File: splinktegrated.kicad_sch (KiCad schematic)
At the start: 60 parts, among them J1 USB_C_Receptacle_USB2.0, J10 NA_Ribbon, J11 NA_Serial, J12 NA_Conn_01x04_Female, J14 Cirque, J16 Conn_01x01_Socket, J17 Conn_01x01_Socket, J2 NA_Conn_01x04_Female, J3 NA_Conn_01x04_Female, J4 NA_Conn_01x04_Female, J5 Conn_01x02, J6 Cirque, J7 NA_trackball, J8 NA_Ribbon, J9 NA_RGB, SW1 NA_SW_SPST, SW2 NA_SW_SPST, U1 RP2040, U2 USBLC6-2P6, U3 XC6210B332MR-G, U4 USBLC6-2P6, U5 W25Q128JVS, Y1 Crystal_GND24

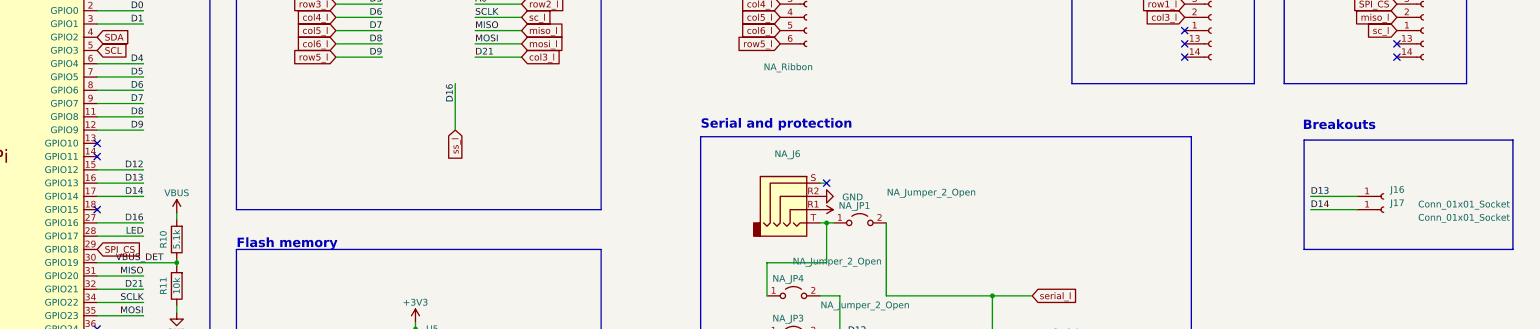
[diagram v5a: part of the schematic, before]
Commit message: add 2 breakout pins
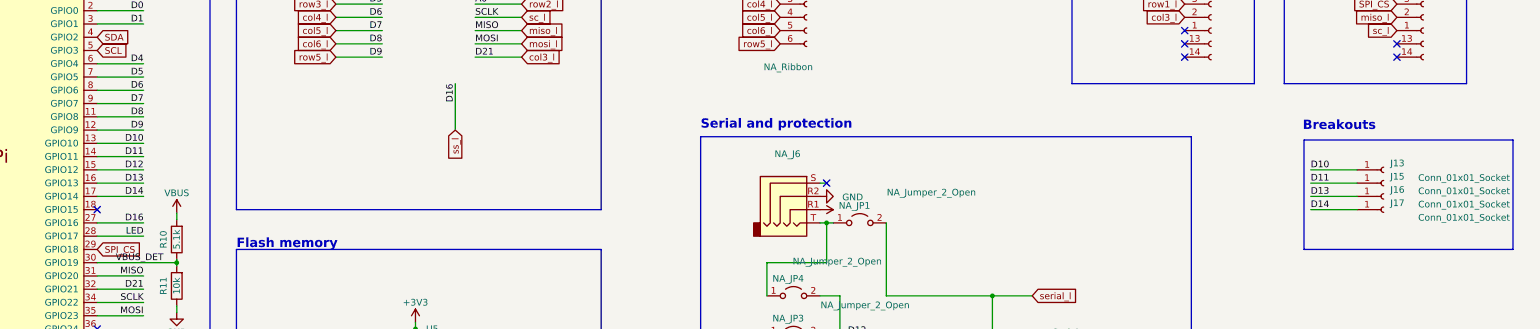
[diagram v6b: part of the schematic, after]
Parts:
- added J13, J15: Conn_01x01_Socket, local-libraries:PinHeader_1x01_P1.27mm_Vertical, symbol Connector:Conn_01x01_Socket
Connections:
- net D10: now reaches U1.13 (GPIO10)
- net D10: now also J13.1 (Pin_1)
- net D11: now reaches U1.14 (GPIO11)
- net D11: now also J15.1 (Pin_1)
- no-connect marks 18 -> 16
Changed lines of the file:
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@@
 	)
 	(no_connect
-		(at 182.88 83.82)
-	)
-	(no_connect
 		(at -88.9 60.96)
 	)
@@
 	)
 	(no_connect
-		(at 182.88 86.36)
-	)
-	(no_connect
 		(at 391.16 67.31)
 	)
@@
 	(wire
 		(pts
+			(xy 182.88 86.36) (xy 191.77 86.36)
+		)
+		(stroke
+			(width 0)
+			(type default)
+		)
+	)
+	(wire
+		(pts
 			(xy 121.92 185.42) (xy 130.81 185.42)
 		)
@@
 	(wire
 		(pts
+			(xy 424.18 91.44) (xy 415.29 91.44)
+		)
+		(stroke
+			(width 0)
+			(type default)
+		)
+	)
+	(wire
+		(pts
 			(xy -85.09 48.26) (xy -88.9 48.26)
 		)
@@
 	(wire
 		(pts
+			(xy 424.18 88.9) (xy 415.29 88.9)
+		)
+		(stroke
+			(width 0)
+			(type default)
+		)
+	)
+	(wire
+		(pts
 			(xy 138.43 40.64) (xy 138.43 38.1)
 		)
@@
 	(wire
 		(pts
+			(xy 182.88 83.82) (xy 191.77 83.82)
+		)
+		(stroke
+			(width 0)
+			(type default)
+		)
+	)
+	(wire
+		(pts
 			(xy 264.16 67.31) (xy 255.27 67.31)
 		)
@@
 		)
 	)
+	(label "D11"
+		(at 415.29 91.44 0)
+		(fields_autoplaced yes)
+		(effects
+			(font
+				(size 1.27 1.27)
+			)
+			(justify left bottom)
+		)
+	)
 	(label "D14"
 		(at 191.77 93.98 180)
@@
 		)
 	)
+	(label "D10"
+		(at 415.29 88.9 0)
+		(fields_autoplaced yes)
+		(effects
+			(font
+				(size 1.27 1.27)
+			)
+			(justify left bottom)
+		)
+	)
 	(label "QSPI_~{CS}"
 		(at 46.355 160.655 0)
@@
 		)
 	)
+	(label "D10"
+		(at 191.77 83.82 180)
+		(fields_autoplaced yes)
+		(effects
+			(font
+				(size 1.27 1.27)
+			)
+			(justify right bottom)
+		)
+	)
 	(label "D-_daughter"
 		(at -103.505 113.03 180)
@@
 		)
 	)
+	(label "D11"
+		(at 191.77 86.36 180)
+		(fields_autoplaced yes)
+		(effects
+			(font
+				(size 1.27 1.27)
+			)
+			(justify right bottom)
+		)
+	)
 	(global_label "row5_l"
 		(shape input)
@@
 	)
 	(symbol
+		(lib_id "Connector:Conn_01x01_Socket")
+		(at 429.26 88.9 0)
+		(unit 1)
+		(exclude_from_sim no)
+		(in_bom yes)
+		(on_board yes)
+		(dnp no)
+		(property "Reference" "J13"
+			(at 430.53 87.6299 0)
+			(effects
+				(font
+					(size 1.27 1.27)
+				)
+				(justify left)
+			)
+		)
+		(property "Value" "Conn_01x01_Socket"
+			(at 435.864 90.424 0)
+			(effects
+				(font
+					(size 1.27 1.27)
+				)
+				(justify left)
+			)
+		)
+		(property "Footprint" "local-libraries:PinHeader_1x01_P1.27mm_Vertical"
+			(at 429.26 88.9 0)
+			(effects
+				(font
+					(size 1.27 1.27)
+				)
+				(hide yes)
+			)
+		)
+		(property "Datasheet" "~"
+			(at 429.26 88.9 0)
+			(effects
+				(font
+					(size 1.27 1.27)
+				)
+				(hide yes)
+			)
+		)
+		(property "Description" "Generic connector, single row, 01x01, script generated"
+			(at 429.26 88.9 0)
+			(effects
+				(font
+					(size 1.27 1.27)
+				)
+				(hide yes)
+			)
+		)
+		(pin "1"
+		)
+		(instances
+			(project "splinktegrated"
+				(path "/7353e96a-343a-4876-b497-b1d205a14d97"
+					(reference "J13")
+					(unit 1)
+				)
+			)
+		)
+	)
+	(symbol
 		(lib_id "Connector:USB_C_Receptacle_USB2.0")
 		(at -104.14 48.26 0)
@@
 					(unit 1)
 				)
+			)
+		)
+	)
+	(symbol
+		(lib_id "Connector:Conn_01x01_Socket")
+		(at 429.26 91.44 0)
+		(unit 1)
+		(exclude_from_sim no)
+		(in_bom yes)
+		(on_board yes)
+		(dnp no)
+		(property "Reference" "J15"
+			(at 430.53 90.1699 0)
+			(effects
+				(font
+					(size 1.27 1.27)
+				)
+				(justify left)
+			)
+		)
+		(property "Value" "Conn_01x01_Socket"
+			(at 435.864 92.964 0)
+			(effects
+				(font
+					(size 1.27 1.27)
+				)
+				(justify left)
+			)
+		)
+		(property "Footprint" "local-libraries:PinHeader_1x01_P1.27mm_Vertical"
+			(at 429.26 91.44 0)
+			(effects
+				(font
+					(size 1.27 1.27)
+				)
+				(hide yes)
+			)
+		)
+		(property "Datasheet" "~"
+			(at 429.26 91.44 0)
+			(effects
+				(font
+					(size 1.27 1.27)
+				)
+				(hide yes)
+			)
+		)
+		(property "Description" "Generic connector, single row, 01x01, script generated"
+			(at 429.26 91.44 0)
+			(effects
+				(font
+					(size 1.27 1.27)
+				)
+				(hide yes)
+			)
+		)
+		(pin "1"
+		)
+		(instances
+			(project "splinktegrated"
+				(path "/7353e96a-343a-4876-b497-b1d205a14d97"
+					(reference "J15")
+					(unit 1)
+				)

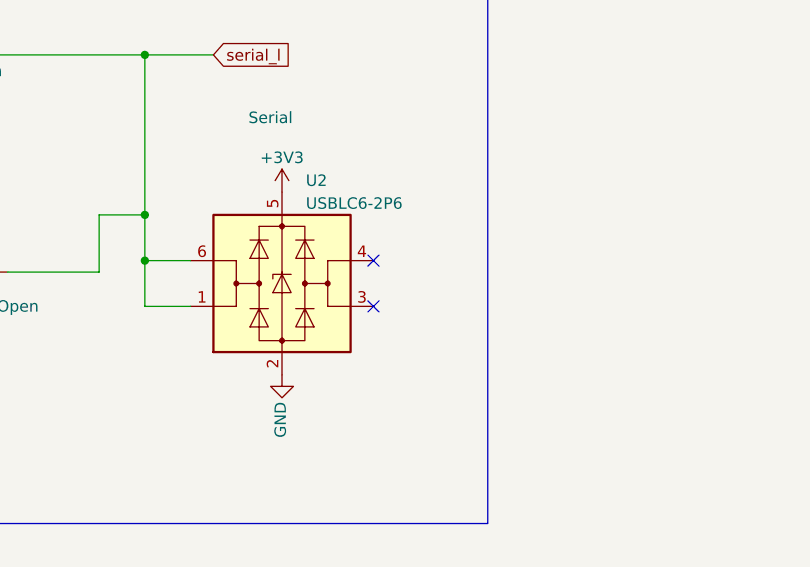
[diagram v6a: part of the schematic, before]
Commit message: add ESD protection on second serial pin
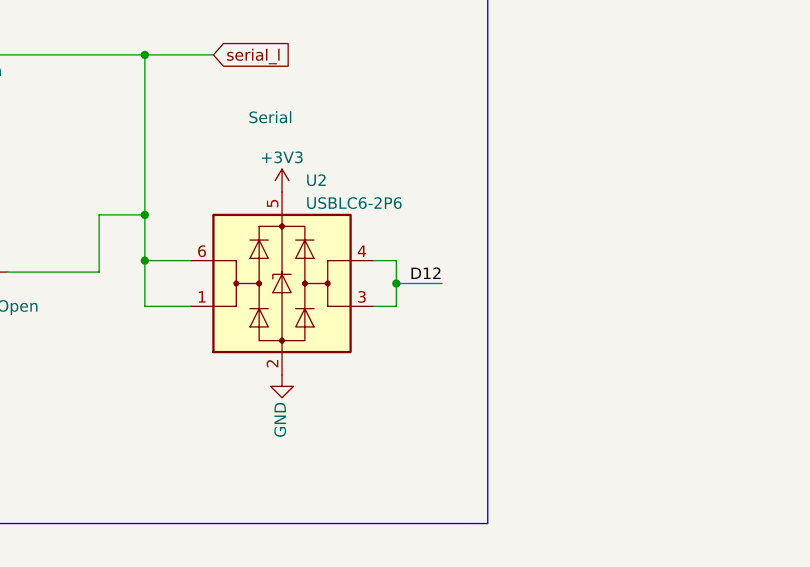
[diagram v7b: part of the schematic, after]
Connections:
- net D12: now also U2.3 (I/O2), U2.4 (I/O2)
- no-connect marks 16 -> 14
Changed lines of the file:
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@@
 	)
 	(junction
+		(at 382.27 138.43)
+		(diameter 0)
+		(color 0 0 0 0)
+	)
+	(junction
 		(at 162.56 38.1)
 		(diameter 0)
@@
 	)
 	(no_connect
-		(at 379.73 135.89)
-	)
-	(no_connect
 		(at 391.16 64.77)
 	)
@@
 	)
 	(no_connect
-		(at 379.73 140.97)
-	)
-	(no_connect
 		(at 391.16 67.31)
 	)
@@
 	(wire
 		(pts
+			(xy 379.73 140.97) (xy 382.27 140.97)
+		)
+		(stroke
+			(width 0)
+			(type default)
+		)
+	)
+	(wire
+		(pts
 			(xy 58.42 113.03) (xy 58.42 118.11)
 		)
@@
 	(wire
 		(pts
+			(xy 382.27 135.89) (xy 382.27 138.43)
+		)
+		(stroke
+			(width 0)
+			(type default)
+		)
+	)
+	(wire
+		(pts
 			(xy 218.44 134.62) (xy 231.14 134.62)
 		)
@@
 	(wire
 		(pts
+			(xy 379.73 135.89) (xy 382.27 135.89)
+		)
+		(stroke
+			(width 0)
+			(type default)
+		)
+	)
+	(wire
+		(pts
 			(xy 182.88 132.08) (xy 191.77 132.08)
 		)
@@
 	(wire
 		(pts
+			(xy 382.27 138.43) (xy 387.35 138.43)
+		)
+		(stroke
+			(width 0)
+			(type default)
+		)
+	)
+	(wire
+		(pts
 			(xy 46.99 127) (xy 46.99 128.27)
 		)
@@
 	(wire
 		(pts
+			(xy 382.27 140.97) (xy 382.27 138.43)
+		)
+		(stroke
+			(width 0)
+			(type default)
+		)
+	)
+	(wire
+		(pts
 			(xy 134.62 36.83) (xy 134.62 40.64)
 		)
@@
 		(fields_autoplaced yes)
 		(effects
+			(font
+				(size 1.27 1.27)
+			)
+			(justify right bottom)
+		)
+	)
+	(label "D12"
+		(at 387.35 138.43 180)
+		(fields_autoplaced yes)
+		(effects

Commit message: zones
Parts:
- NA_JP3, NA_JP4, NA_JP5: footprint local-libraries:SolderJumper-2_P1.3mm_Open_RoundedPad1.0x1.5mm -> local-libraries:SolderJumper-2_P1.3mm_Open_TrianglePad1.0x1.5mm
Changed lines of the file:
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@@
 			)
 		)
-		(property "Footprint" "local-libraries:SolderJumper-2_P1.3mm_Open_RoundedPad1.0x1.5mm"
+		(property "Footprint" "local-libraries:SolderJumper-2_P1.3mm_Open_TrianglePad1.0x1.5mm"
 			(at 316.23 120.65 0)
 			(effects
@@
 			)
 		)
-		(property "Footprint" "local-libraries:SolderJumper-2_P1.3mm_Open_RoundedPad1.0x1.5mm"
+		(property "Footprint" "local-libraries:SolderJumper-2_P1.3mm_Open_TrianglePad1.0x1.5mm"
 			(at 426.72 46.99 0)
 			(effects
@@
 			)
 		)
-		(property "Footprint" "local-libraries:SolderJumper-2_P1.3mm_Open_RoundedPad1.0x1.5mm"
+		(property "Footprint" "local-libraries:SolderJumper-2_P1.3mm_Open_TrianglePad1.0x1.5mm"
 			(at 316.23 113.03 0)
 			(effects
